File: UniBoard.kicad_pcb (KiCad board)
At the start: 2 copper layers, 89 x 93.3 mm, 7 parts, among them J1 UniSat_BUS_40

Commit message: added silk screen
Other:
- board text added: "."
- board text added: "1"
- board text added: "2"
- board text added: "39"
- board text added: "3V3"
- board text added: "40"
- board text added: "5"
- board text added: "7V4"
- board text added: "BUSY"
- board text added: "CH1"
- board text added: "CH2"
- board text added: "CH3"
- board text added: "CH4"
- board text added: "CH5"
- board text added: "GND"
- board text added: "I2C SCL"
- board text added: "I2C SDA"
- board text added: "INT"
- board text added: "RFU"
- board text added: "RS485 A"
- board text added: "RS485 B"

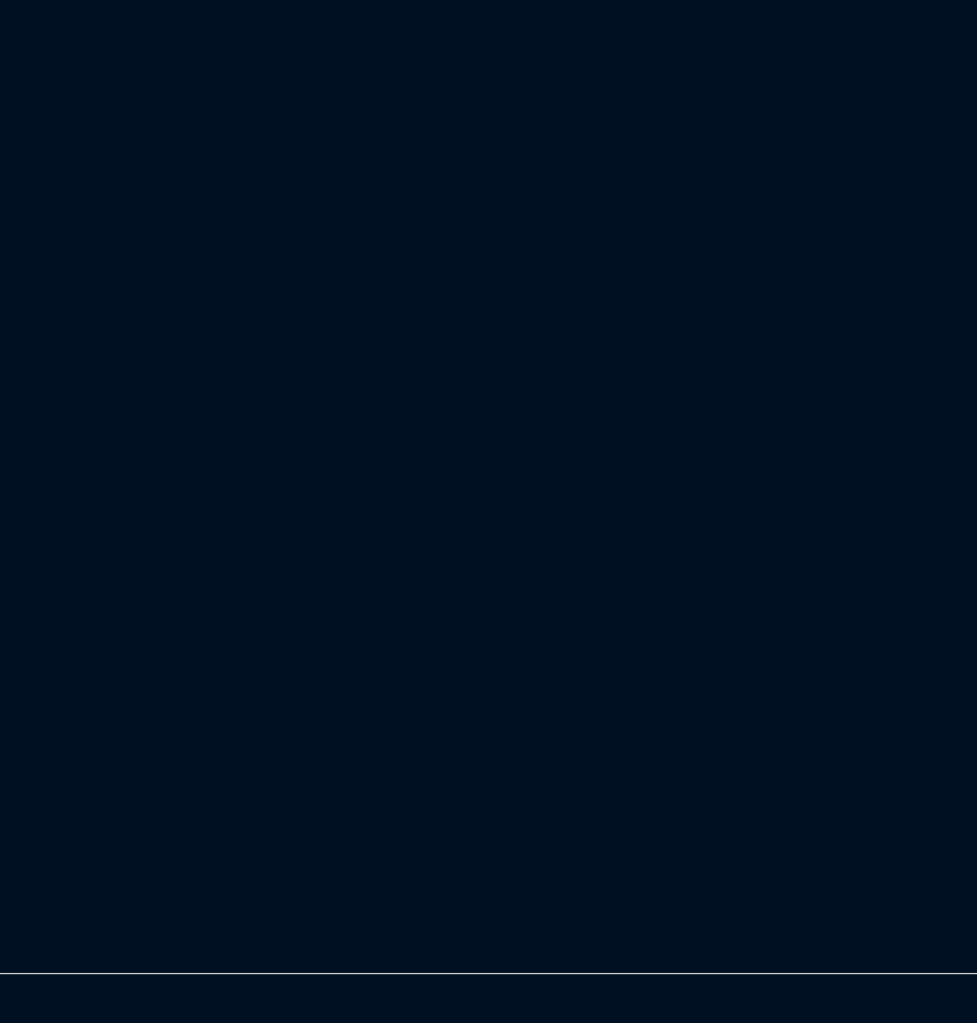
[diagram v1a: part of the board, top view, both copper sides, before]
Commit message: logog and text added
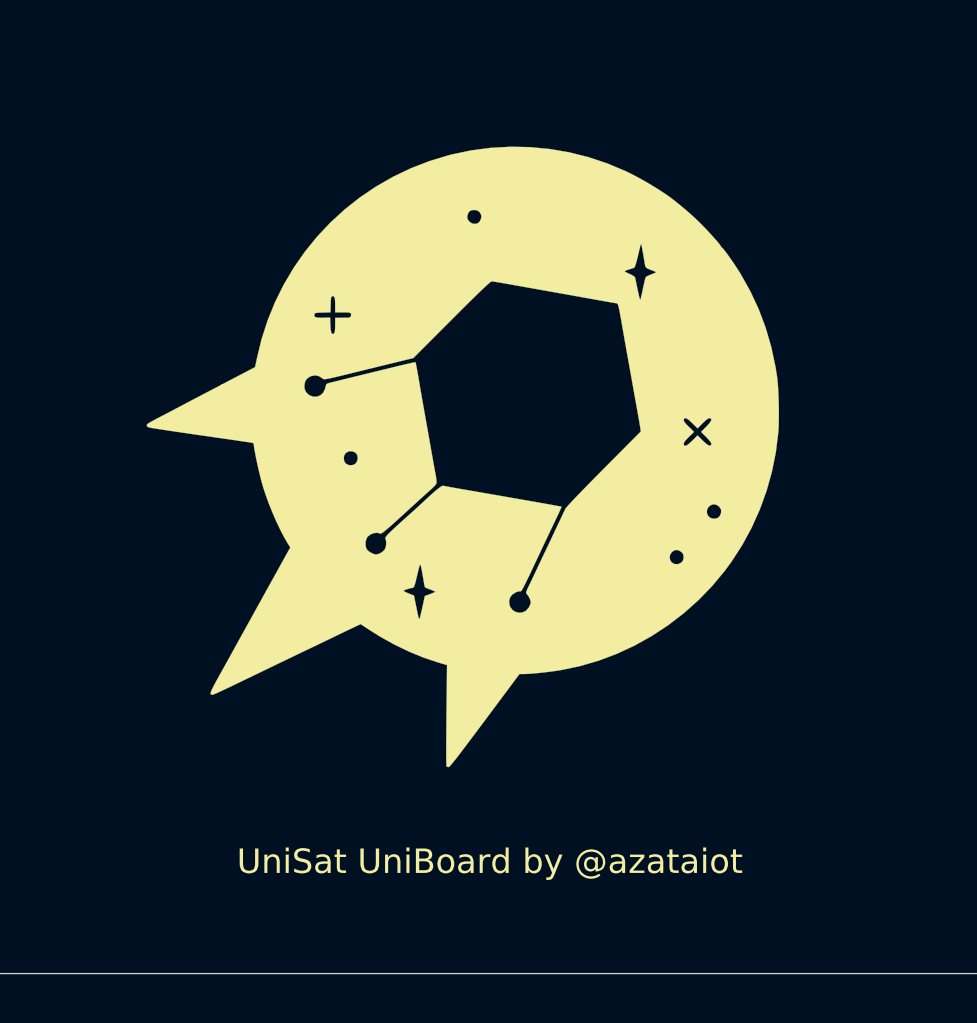
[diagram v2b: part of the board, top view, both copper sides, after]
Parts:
- added G***: LOGO, UniBoard:Logo, F.Cu at (145.5, 116.5)
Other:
- board text added: "UniSat UniBoard by @azataiot"
- board text added: "https://unisat.kz"
